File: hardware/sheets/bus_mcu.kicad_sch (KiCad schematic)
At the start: 60 parts, among them M1 Core2350B (0MB PSRAM), U10 74HC161, U11 74HC161, U12 74HC165, U14 74HC244, U15 74HC244, U16 74HC244, U17 74LVC04A, U18 74HC08, U19 74HC165, U20 74HC165, U7 74HC161, U8 74HC161, U9 74HC161

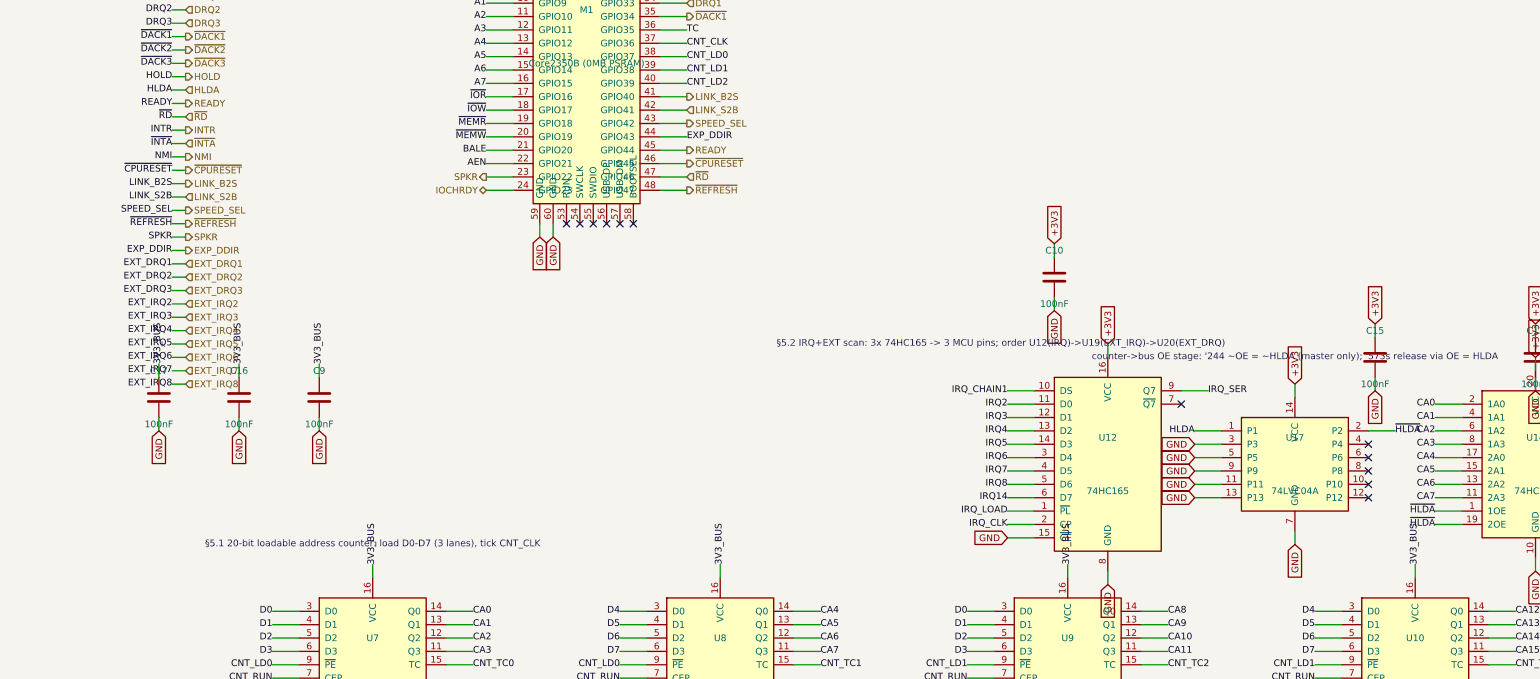
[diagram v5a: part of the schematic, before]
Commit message: bus_mcu: delete U17 (74LVC04A, 1/6 gates) -- HLDA inverter moves to parallel's spare gate
The HLDA -> ~{HLDA} inversion for the counter '244s now lives on the
parallel sheet's spare 74AHC14 Schmitt gate (U9.1, freed by the decode
centralization) -- the board's only spare 5V-tolerant inverter, which is
what HLDA (raw 5V V20 output) requires. ~{HLDA} joins mxbus.PRIV_CPU and
crosses as an interface net; park-safety unchanged (R18 parks HLDA low,
~{HLDA} idles high, '244s off during MCU-Hi-Z). U17 + its decoupler
deleted; the orphaned 74LVC04A parts.py line (C282341) removed. Board
454 comps / 92 ICs. Also sweeps stale JP-number refs left in the
parallel/storage/com_port docstrings from the jumper renumber.

Co-Authored-By: Claude Fable 5 <noreply@anthropic.com>
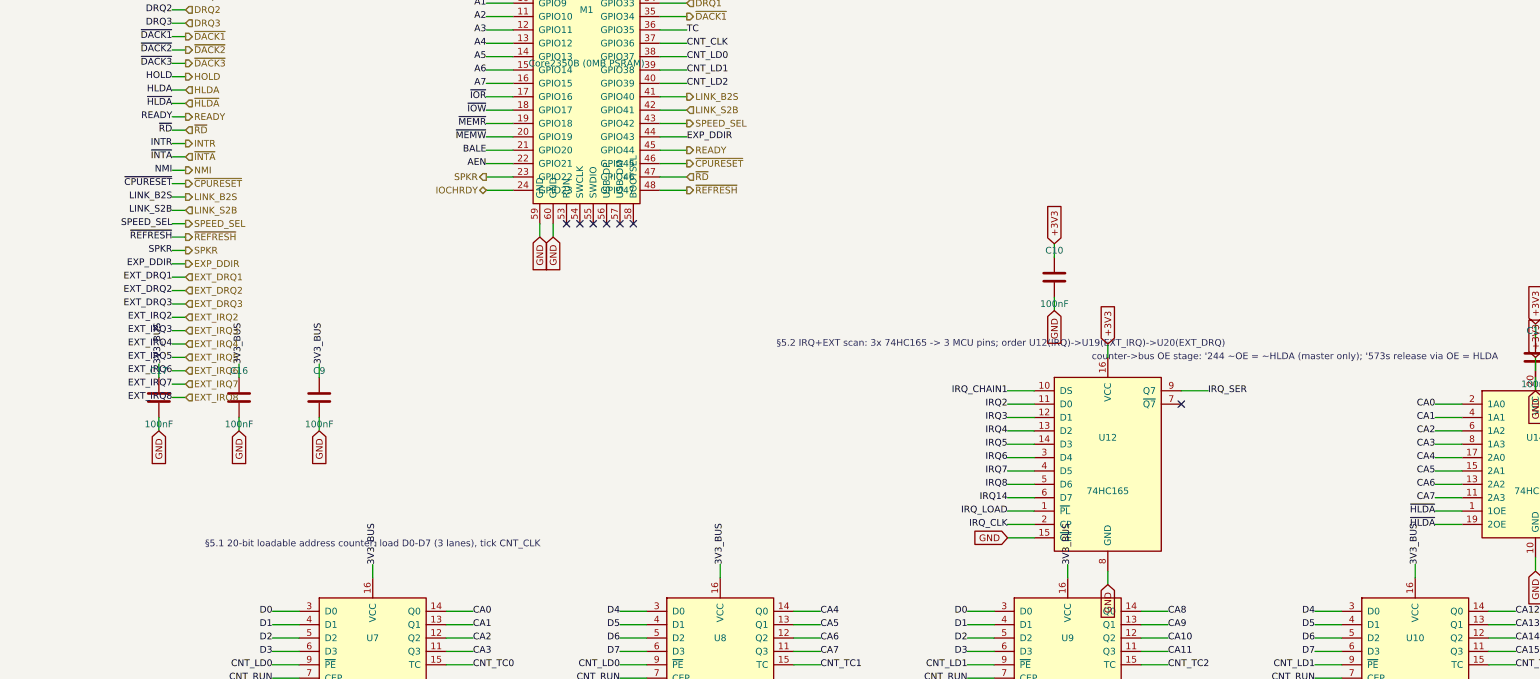
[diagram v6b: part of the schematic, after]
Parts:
- removed C15: 100nF, Capacitor_SMD:C_0603_1608Metric, symbol Device:C
- removed U17: 74LVC04A, Package_SO:SOIC-14_3.9x8.7mm_P1.27mm, symbol mini-xt:74HCT04
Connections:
- no-connect marks 23 -> 18

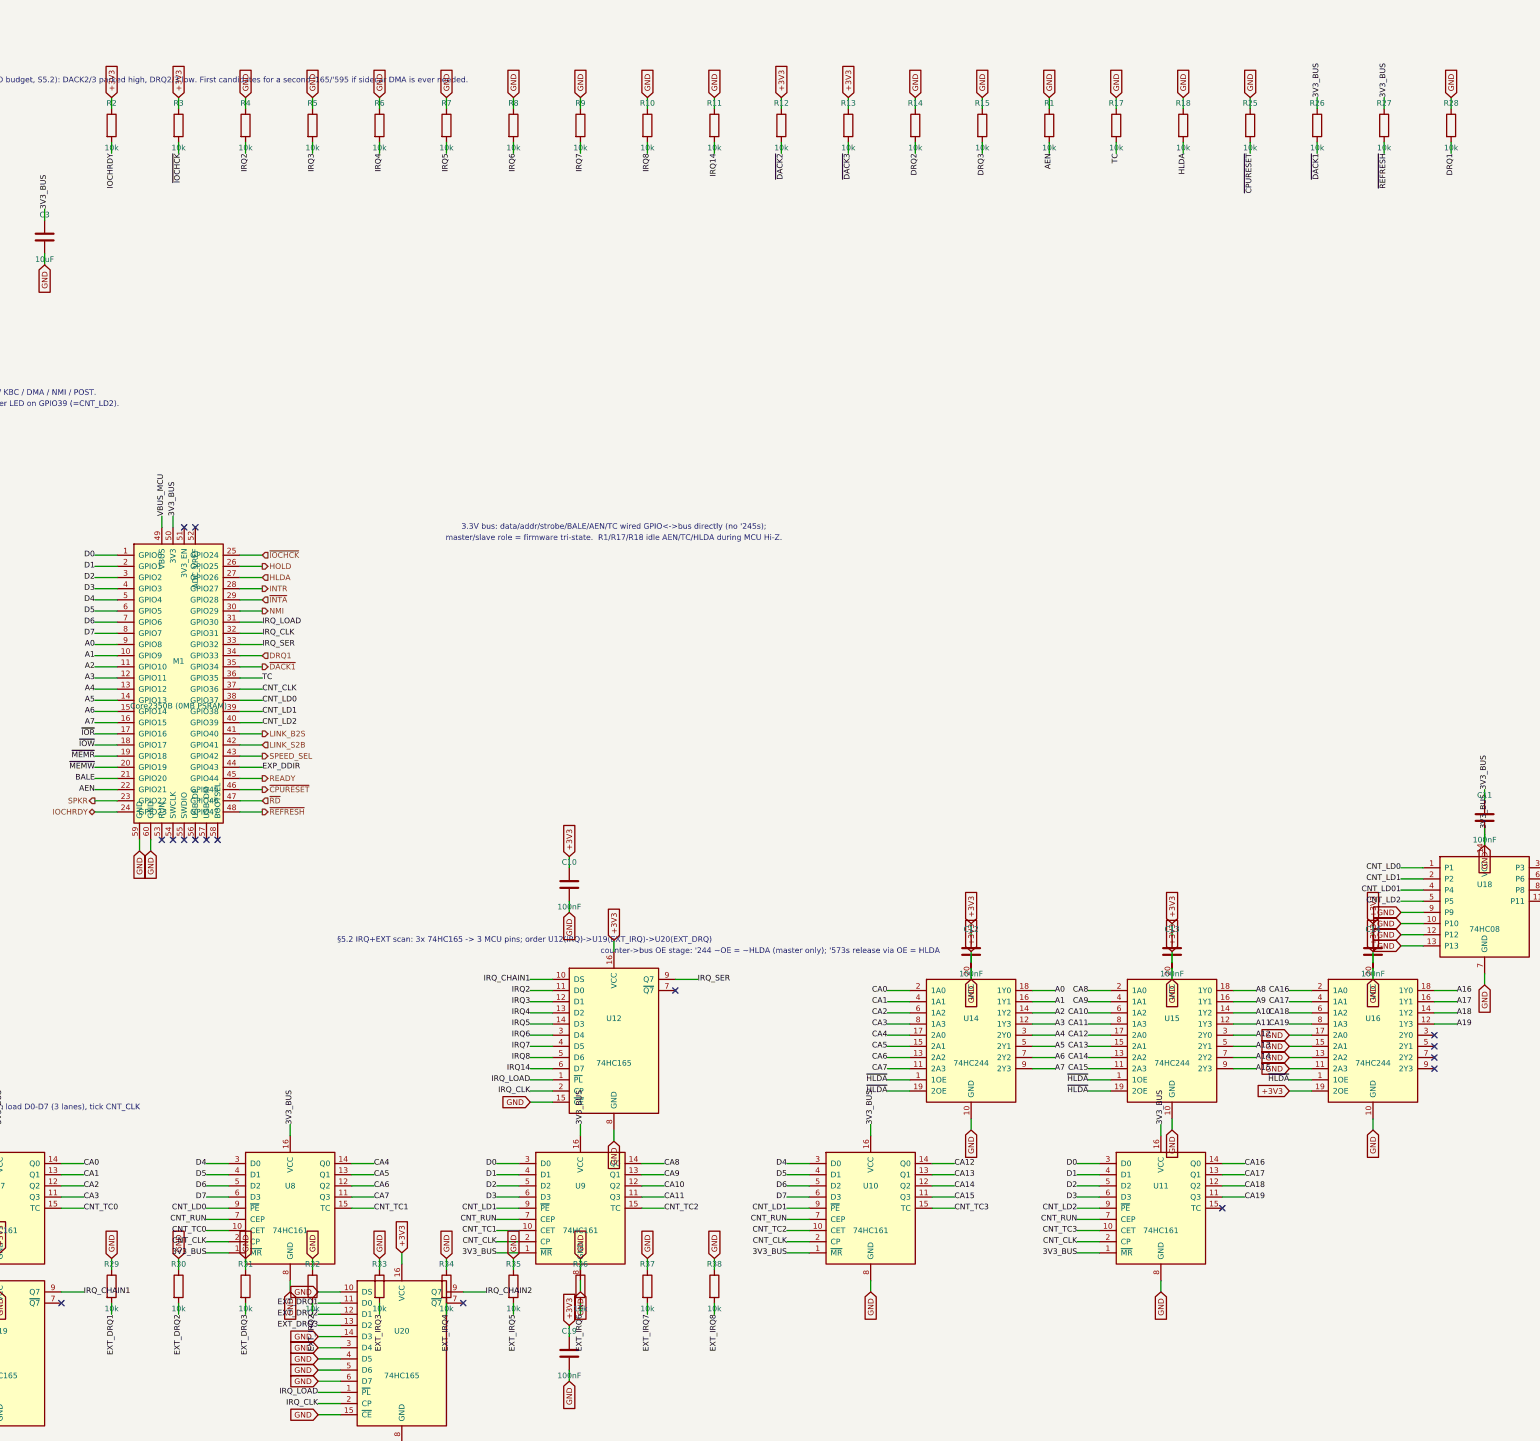
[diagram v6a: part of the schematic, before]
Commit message: Passives: basic-library audit + 4x resistor-array pull consolidation
Audit: every discrete R/C value was already JLC basic except the ferrite
beads -- swapped to basic Murata BLM18PG121SN1D (C14709, 120R@100MHz,
same family/role). The 100uF electrolytic and buck inductor stay
extended (zero fee-free parts exist in those subcategories). Pruned the
orphaned 5V-era 47nF/330nF MAX3241 cap entries.

Pull consolidation: 65 discrete 10k/4.7k rail pulls across 8 sheets
collapse into 18 basic 4-element isolated arrays (4D03WGJ0103T5E /
4D03WGJ0472T5E, element k = pins k/9-k; new mxbus.r_pack4 helper).
Isolated elements let packs mix rails; every net keeps its exact rail
and semantics (verified element-by-element in the netlist). RC/divider/
series/I2C resistors stay discrete. Board 452 -> 406 components; also
de-risks the sole basic 10k 0603 line (0 stock at audit). Audit
recorded in jlcpcb-sourcing.md.

Co-Authored-By: Claude Fable 5 <noreply@anthropic.com>
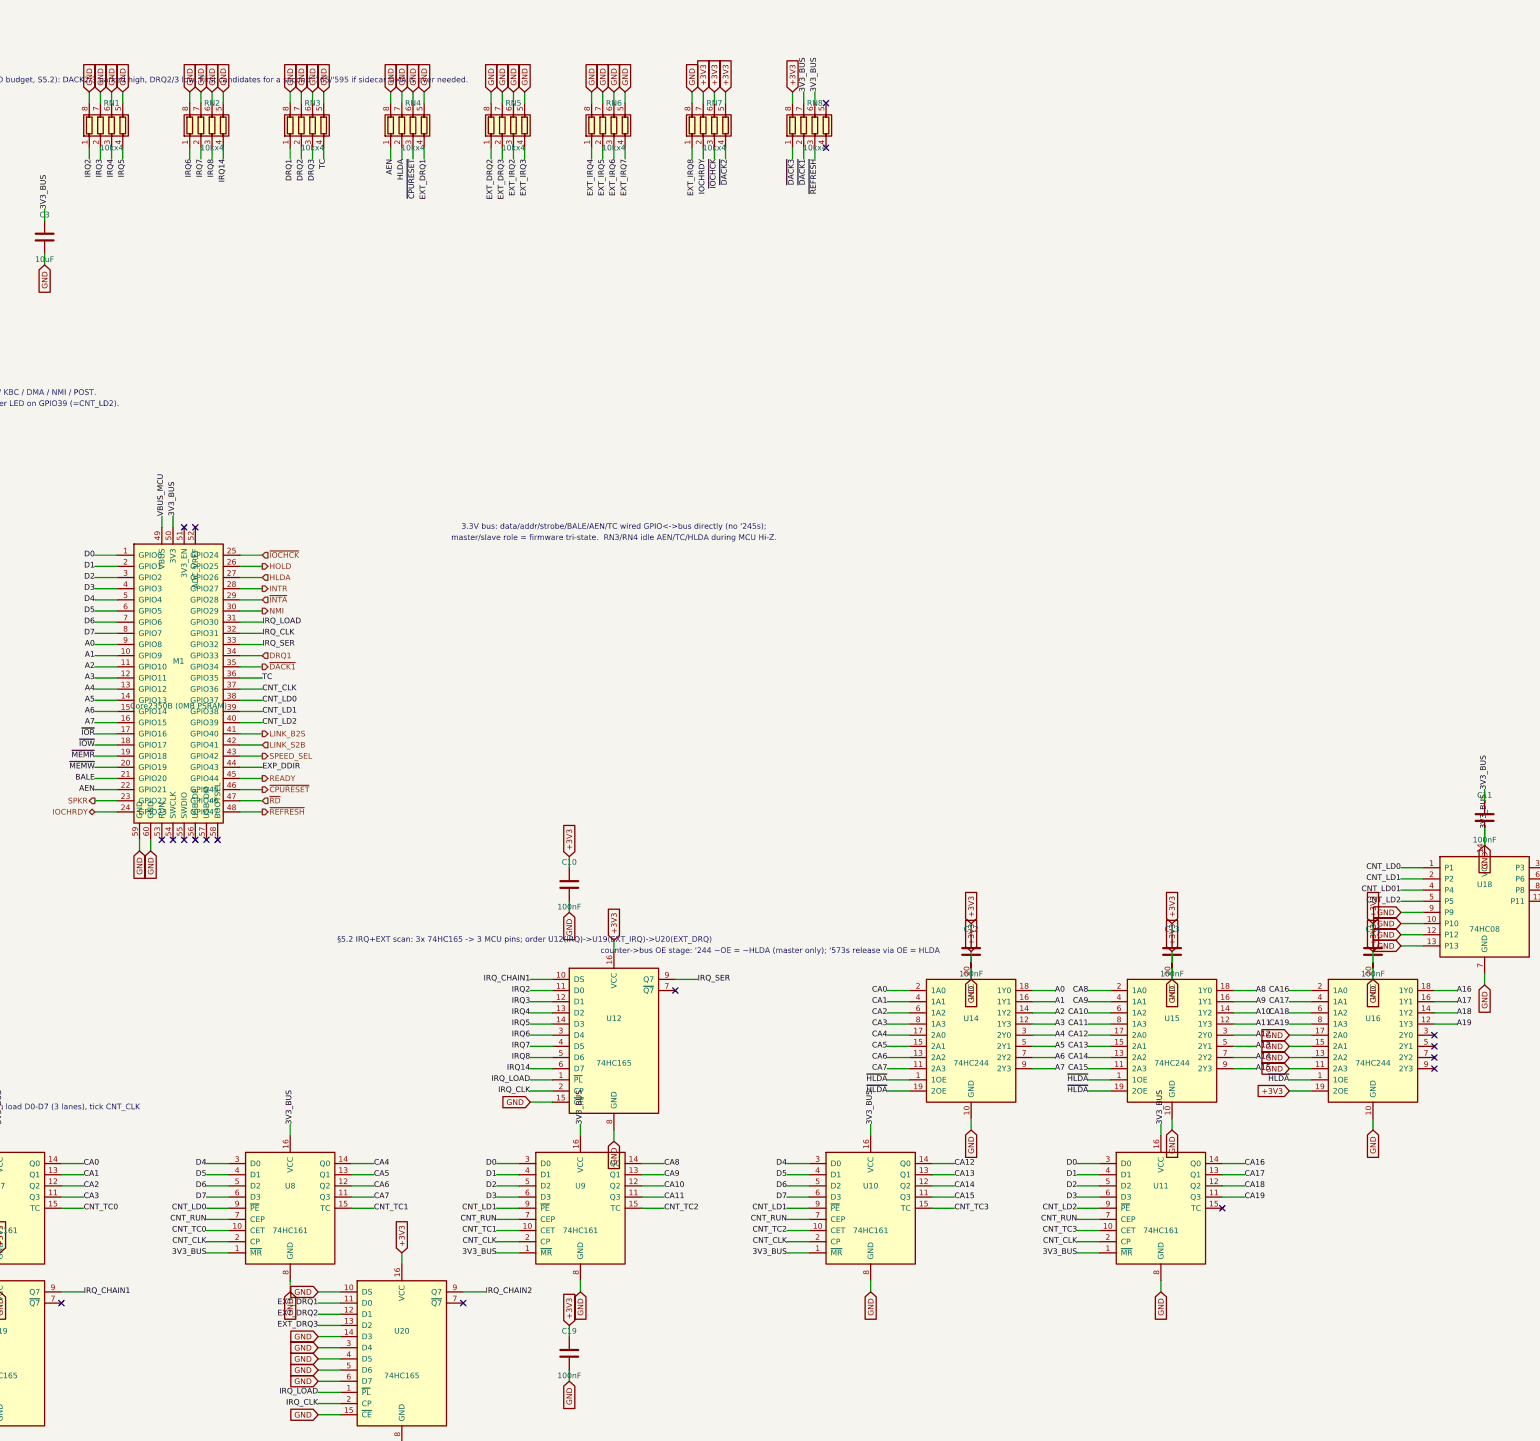
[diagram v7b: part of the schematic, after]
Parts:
- removed R1, R10, R11, R12, R13, R14, R15, R17, R18, R25, R26, R27, R28, R3, R30, R31, R32, R33, R34, R35, R36, R37, R38, R4, R5, R6, R7, R8, R9: 10k, Resistor_SMD:R_0603_1608Metric, symbol Device:R
- added RN2, RN3, RN4, RN5, RN7, RN8: 10kx4, Resistor_SMD:R_Array_Convex_4x0603, symbol Device:R_Pack04
- RN1: renamed from R2; value 10k -> 10kx4; footprint Resistor_SMD:R_0603_1608Metric -> Resistor_SMD:R_Array_Convex_4x0603; symbol Device:R -> Device:R_Pack04; LCSC Part Num C25804 -> C29718
- RN6: renamed from R29; value 10k -> 10kx4; footprint Resistor_SMD:R_0603_1608Metric -> Resistor_SMD:R_Array_Convex_4x0603; symbol Device:R -> Device:R_Pack04; LCSC Part Num C25804 -> C29718
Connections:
- net +3V3: now also RN7.5 (R4.2), RN7.6 (R3.2), RN7.7 (R2.2), RN8.8 (R1.2); no longer RN1.1
- net AEN: now also RN4.1 (R1.1)
- net DRQ1: now also RN3.1 (R1.1)
- net DRQ2: now also RN3.2 (R2.1)
- net DRQ3: now also RN3.3 (R3.1)
- net EXT_DRQ1: now also RN4.4 (R4.1); no longer RN6.2
- net EXT_DRQ2: now also RN5.1 (R1.1)
- net EXT_DRQ3: now also RN5.2 (R2.1)
- net EXT_IRQ2: now also RN5.3 (R3.1)
- net EXT_IRQ3: now also RN5.4 (R4.1)
- net EXT_IRQ4: now also RN6.1 (R1.1)
- net EXT_IRQ5: now also RN6.2 (R2.1)
- net EXT_IRQ6: now also RN6.3 (R3.1)
- net EXT_IRQ7: now also RN6.4 (R4.1)
- net EXT_IRQ8: now also RN7.1 (R1.1)
- net GND: now also RN1.5 (R4.2), RN1.6 (R3.2), RN1.7 (R2.2), RN1.8 (R1.2), RN6.5 (R4.2), RN6.6 (R3.2), RN6.7 (R2.2), RN6.8 (R1.2), RN2.5 (R4.2), RN2.6 (R3.2), RN2.7 (R2.2), RN2.8 (R1.2), RN3.5 (R4.2), RN3.6 (R3.2), RN3.7 (R2.2), RN3.8 (R1.2), RN4.5 (R4.2), RN4.6 (R3.2), RN4.7 (R2.2), RN4.8 (R1.2), RN5.5 (R4.2), RN5.6 (R3.2), RN5.7 (R2.2), RN5.8 (R1.2), RN7.8 (R1.2), RN8.6 (R3.2), RN8.7 (R2.2); no longer RN6.1
- net HLDA: now also RN4.2 (R2.1)
- net IOCHRDY: now also RN7.2 (R2.1); no longer RN1.2
- net IRQ14: now also RN2.4 (R4.1)
- net IRQ2: now also RN1.1 (R1.1)
- net IRQ3: now also RN1.2 (R2.1)
- net IRQ4: now also RN1.3 (R3.1)
- net IRQ5: now also RN1.4 (R4.1)
- net IRQ6: now also RN2.1 (R1.1)
- net IRQ7: now also RN2.2 (R2.1)
- net IRQ8: now also RN2.3 (R3.1)
- net TC: now also RN3.4 (R4.1)
- net ~{CPURESET}: now also RN4.3 (R3.1)
- net ~{DACK1}: now also RN8.2 (R2.1)
- net ~{DACK2}: now also RN7.4 (R4.1)
- net ~{DACK3}: now also RN8.1 (R1.1)
- net ~{IOCHCK}: now also RN7.3 (R3.1)
- net ~{REFRESH}: now also RN8.3 (R3.1)
- no-connect marks 18 -> 20
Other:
- note added: "master/slave role = firmware tri-state. RN3/RN4 idle AEN/TC/HLDA during MCU Hi-Z."
- note removed: "master/slave role = firmware tri-state. R1/R17/R18 idle AEN/TC/HLDA during MCU Hi-Z."

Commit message: ERC to zero: PWR_FLAG on VDD_RTC; retire IRQ6/IRQ8/EXT_IRQ8
Full-project ERC is now 0 errors / 0 warnings, and CLAUDE.md makes that
the standing bar. Two fixes:

- supervisor: PWR_FLAG on VDD_RTC (fed only through the D1/D2 diode-OR,
  so ERC saw no power source driving the PCF8563's VDD).
- IRQ6/IRQ8/EXT_IRQ8 formally retired (resolving the flagged IRQ8
  follow-up): none could ever be driven -- IRQ6 is a firmware floppy
  event (sidecar FDC arrives as EXT_IRQ6), IRQ8's RTC is firmware-
  emulated, EXT_IRQ8 has no header pin. Their '165 lanes tie LOW at the
  same bit positions (firmware scan map unchanged); PRIV_EXP ends at
  EXT_IRQ7; bus_mcu pulls repack 8 -> 7 full arrays. Board 405 comps /
  91 ICs. Docs + notes aligned.

Co-Authored-By: Claude Fable 5 <noreply@anthropic.com>
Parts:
- removed RN8: 10kx4, Resistor_SMD:R_Array_Convex_4x0603, symbol Device:R_Pack04
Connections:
- net +3V3: now also RN6.5 (R4.2), RN6.6 (R3.2), RN7.8 (R1.2); no longer RN7.5 (R4.2), RN7.6 (R3.2)
- net AEN: now also RN3.3 (R3.1); no longer RN4.1 (R1.1)
- net DRQ1: now also RN2.3 (R3.1); no longer RN3.1 (R1.1)
- net DRQ2: now also RN2.4 (R4.1); no longer RN3.2 (R2.1)
- net DRQ3: now also RN3.1 (R1.1); no longer RN3.3 (R3.1)
- net EXT_DRQ1: now also RN4.2 (R2.1); no longer RN4.4 (R4.1)
- net EXT_DRQ2: now also RN4.3 (R3.1); no longer RN5.1 (R1.1)
- net EXT_DRQ3: now also RN4.4 (R4.1); no longer RN5.2 (R2.1)
- net EXT_IRQ2: now also RN5.1 (R1.1); no longer RN5.3 (R3.1)
- net EXT_IRQ3: now also RN5.2 (R2.1); no longer RN5.4 (R4.1)
- net EXT_IRQ4: now also RN5.3 (R3.1); no longer RN6.1 (R1.1)
- net EXT_IRQ5: now also RN5.4 (R4.1); no longer RN6.2 (R2.1)
- net EXT_IRQ6: now also RN6.1 (R1.1); no longer RN6.3 (R3.1)
- net EXT_IRQ7: now also RN6.2 (R2.1); no longer RN6.4 (R4.1)
- net GND: now also RN7.5 (R4.2), RN7.6 (R3.2), U12.3 (D4), U12.5 (D6), U19.5 (D6); no longer RN6.5 (R4.2), RN6.6 (R3.2), RN7.8 (R1.2)
- net HLDA: now also RN3.4 (R4.1); no longer RN4.2 (R2.1)
- net IOCHRDY: now also RN6.3 (R3.1); no longer RN7.2 (R2.1)
- net IRQ14: now also RN2.2 (R2.1); no longer RN2.4 (R4.1)
- net IRQ7: now also RN2.1 (R1.1); no longer RN2.2 (R2.1)
- net TC: now also RN3.2 (R2.1); no longer RN3.4 (R4.1)
- net ~{CPURESET}: now also RN4.1 (R1.1); no longer RN4.3 (R3.1)
- net ~{DACK1}: now also RN7.3 (R3.1)
- net ~{DACK2}: now also RN7.1 (R1.1); no longer RN7.4 (R4.1)
- net ~{DACK3}: now also RN7.2 (R2.1)
- net ~{IOCHCK}: now also RN6.4 (R4.1); no longer RN7.3 (R3.1)
- net ~{REFRESH}: now also RN7.4 (R4.1)
- removed net EXT_IRQ8: RN7.1 (R1.1), U19.5 (D6)
- removed net IRQ6: RN2.1 (R1.1), U12.3 (D4)
- removed net IRQ8: RN2.3 (R3.1), U12.5 (D6)
- no-connect marks 20 -> 18
